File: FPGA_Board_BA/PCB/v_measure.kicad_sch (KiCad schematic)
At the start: 14 parts, among them U12 1819_IS8

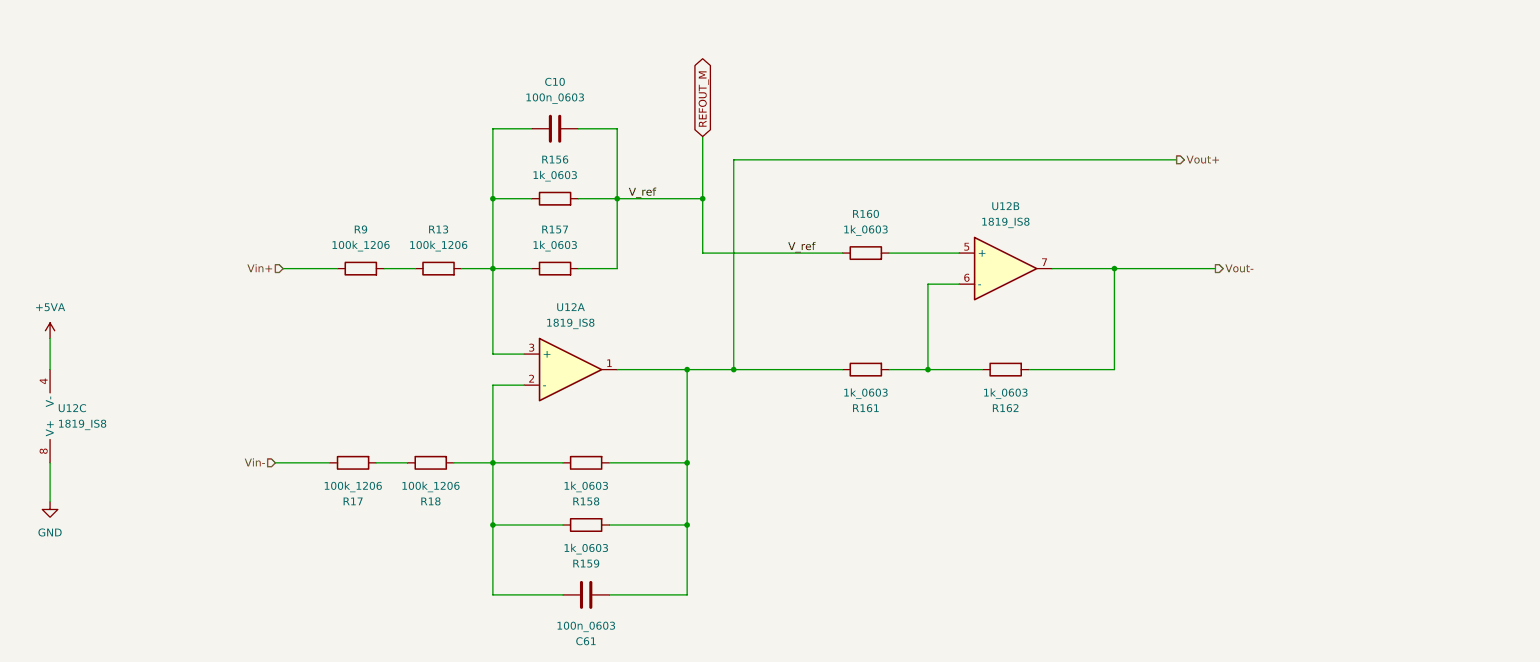
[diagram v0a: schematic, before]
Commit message: started power DCDC layout
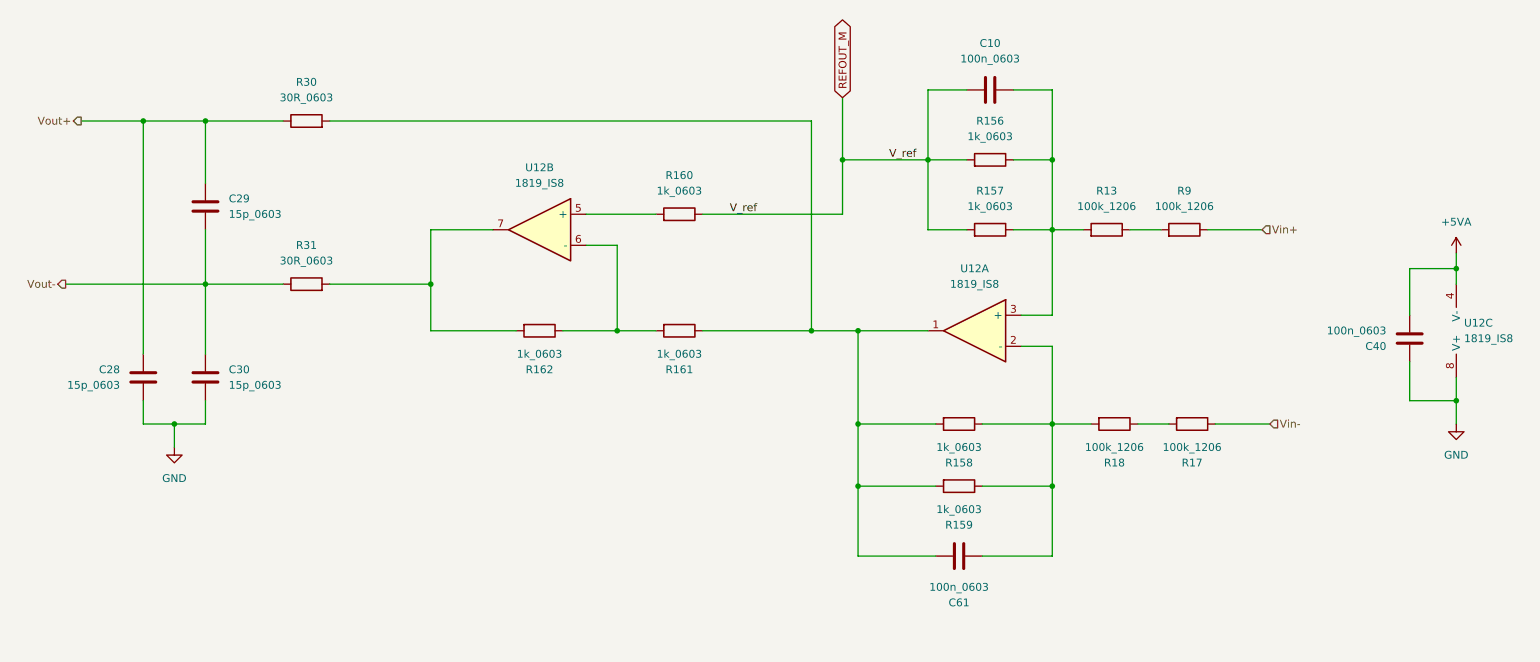
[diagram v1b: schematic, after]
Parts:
- added C28, C29, C30: 15p_0603, WLIB_Capacitor:C_0603, symbol WLIB_C:15p_0603
- added C40: 100n_0603, WLIB_Capacitor:C_0603, symbol WLIB_C:100n_0603
- added R30, R31: 30R_0603, Resistor_SMD:R_0603_1608Metric, symbol WLIB_R:30R_0603
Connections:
- net +5VA: now also C40.2
- net GND: now also C28.2, C30.2, C40.1
- net Vout+: now also C28.1, C29.1, R30.1; no longer C61.2, R158.2, R159.2, R161.1, U12.1
- net Vout-: now also C29.2, C30.1, R31.1; no longer R162.2, U12.7
- new net: R162.2, R31.2, U12.7
- new net: C61.2, R158.2, R159.2, R161.1, R30.2, U12.1
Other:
- moved on the sheet: C10, C61, R13, R156, R157, R158, R159, R160, R161, R162, R17, R18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
